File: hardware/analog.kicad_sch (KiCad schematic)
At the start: 13 parts

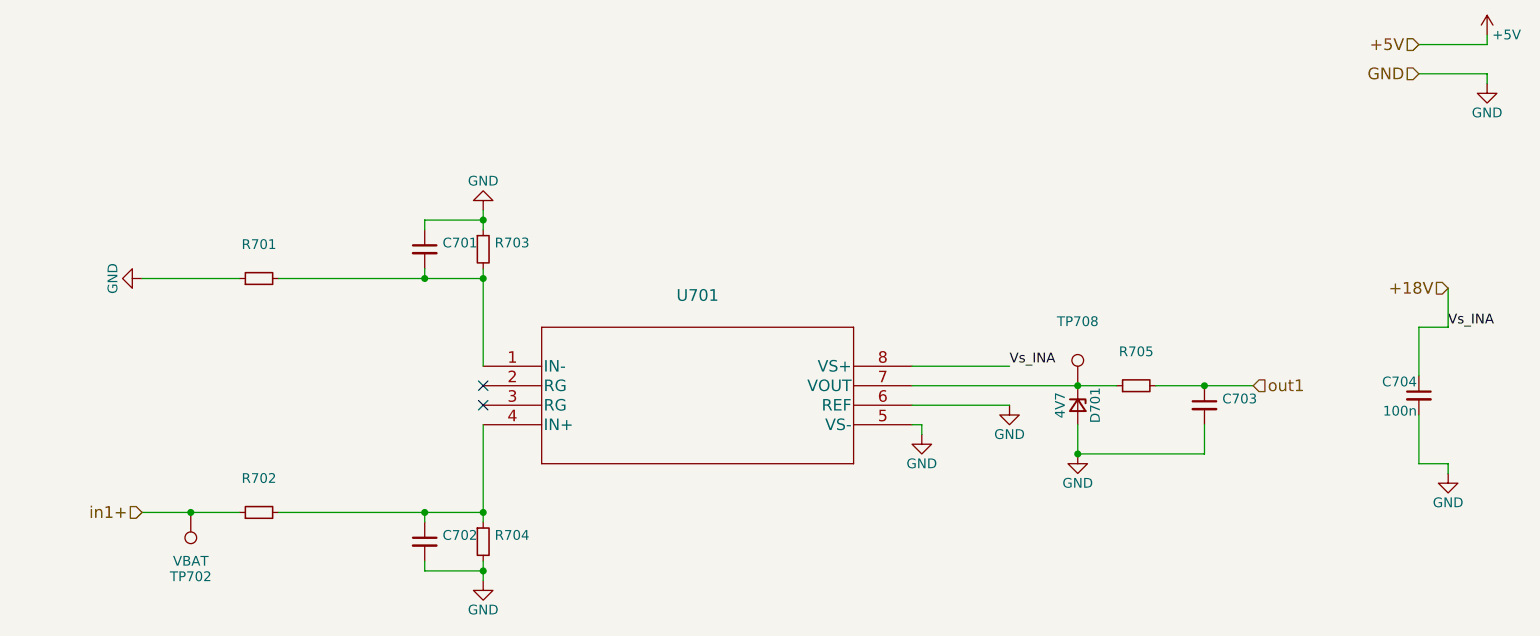
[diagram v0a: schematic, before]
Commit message: hardware: K78L15 to supply INA826 and other changes
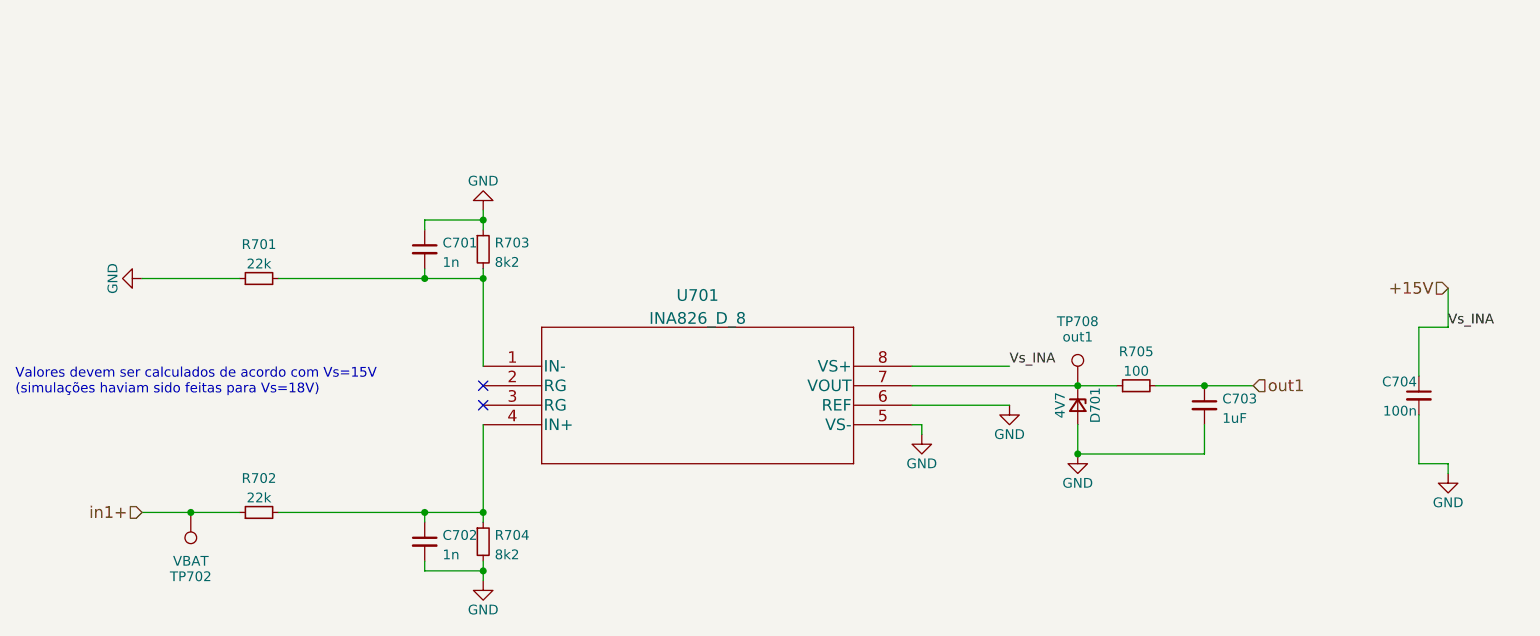
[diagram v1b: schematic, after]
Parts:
- C701, C702: value (none) -> 1n; footprint (none) -> Capacitor_SMD:C_0805_2012Metric_Pad1.18x1.45mm_HandSolder
- C703: value (none) -> 1uF; footprint (none) -> Capacitor_SMD:C_1206_3216Metric_Pad1.33x1.80mm_HandSolder
- R701, R702: value (none) -> 22k; footprint (none) -> Resistor_SMD:R_0805_2012Metric_Pad1.20x1.40mm_HandSolder
- R703, R704: value (none) -> 8k2; footprint (none) -> Resistor_SMD:R_0805_2012Metric_Pad1.20x1.40mm_HandSolder
- R705: value (none) -> 100; footprint (none) -> Resistor_SMD:R_0805_2012Metric_Pad1.20x1.40mm_HandSolder
- TP708: value (none) -> out1; footprint (none) -> TestPoint:TestPoint_Pad_2.0x2.0mm
- U701: value (none) -> INA826_D_8; footprint (none) -> Package_SO:SOIC-8_3.9x4.9mm_P1.27mm
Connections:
- net +18V renamed +15V
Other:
- note added: "Valores devem ser calculados de acordo com Vs=15V (simulações haviam sido feitas para Vs=18V)"
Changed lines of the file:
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@@
-    (stroke (width 0) (type default) (color 0 0 0 0))
-  )
-  (wire (pts (xy 251.46 57.15) (xy 242.57 57.15))
     (stroke (width 0) (type default) (color 0 0 0 0))
   )
@@
     (stroke (width 0) (type default) (color 0 0 0 0))
   )
-  (wire (pts (xy 251.46 55.88) (xy 251.46 57.15))
-    (stroke (width 0) (type default) (color 0 0 0 0))
-  )
   (wire (pts (xy 120.65 125.73) (xy 120.65 124.46))
     (stroke (width 0) (type default) (color 0 0 0 0))
@@
     (stroke (width 0) (type default) (color 0 0 0 0))
   )
-  (wire (pts (xy 251.46 60.96) (xy 251.46 62.23))
-    (stroke (width 0) (type default) (color 0 0 0 0))
-  )
   (wire (pts (xy 82.55 118.11) (xy 88.9 118.11))
     (stroke (width 0) (type default) (color 0 0 0 0))
   )
-  (wire (pts (xy 242.57 60.96) (xy 251.46 60.96))
-    (stroke (width 0) (type default) (color 0 0 0 0))
-  )
   (wire (pts (xy 113.03 125.73) (xy 120.65 125.73))
     (stroke (width 0) (type default) (color 0 0 0 0))
@@
   (wire (pts (xy 246.38 111.76) (xy 242.57 111.76))
     (stroke (width 0) (type default) (color 0 0 0 0))
+  )
+  (text "Valores devem ser calculados de acordo com Vs=15V\n(simulações haviam sido feitas para Vs=18V)"
+    (at 59.69 102.87 0)
+    (effects (font (size 1.27 1.27)) (justify left bottom))
   )
   (label "Vs_INA" (at 246.38 93.98 0)
@@
     (effects (font (size 1.524 1.524)) (justify right))
   )
-  (hierarchical_label "+5V" (shape input) (at 242.57 57.15 180)
-    (effects (font (size 1.524 1.524)) (justify right))
-  )
-  (hierarchical_label "+18V" (shape input) (at 246.38 88.9 180)
-    (effects (font (size 1.524 1.524)) (justify right))
-  )
-  (hierarchical_label "GND" (shape input) (at 242.57 60.96 180)
+  (hierarchical_label "+15V" (shape input) (at 246.38 88.9 180)
     (effects (font (size 1.524 1.524)) (justify right))
   )
@@
     (in_bom yes) (on_board yes) (fields_autoplaced)
     (property "Reference" "R702" (id 0) (at 91.44 113.6736 90))
-    (property "Value" "" (id 1) (at 91.44 116.2105 90))
-    (property "Footprint" "" (id 2) (at 91.44 118.11 0)
+    (property "Value" "22k" (id 1) (at 91.44 116.2105 90))
+    (property "Footprint" "Resistor_SMD:R_0805_2012Metric_Pad1.20x1.40mm_HandSolder" (id 2) (at 91.44 118.11 0)
       (effects (font (size 1.27 1.27)) hide)
     )
@@
       (effects (font (size 1.524 1.524)))
     )
-    (property "Value" "" (id 1) (at 148.59 92.8258 0)
+    (property "Value" "INA826_D_8" (id 1) (at 148.59 92.8258 0)
       (effects (font (size 1.524 1.524)))
     )
-    (property "Footprint" "" (id 2) (at 148.59 92.964 0)
+    (property "Footprint" "Package_SO:SOIC-8_3.9x4.9mm_P1.27mm" (id 2) (at 148.59 92.964 0)
       (effects (font (size 1.524 1.524)) hide)
     )
@@
       (effects (font (size 1.27 1.27)) (justify left))
     )
-    (property "Value" "" (id 1) (at 115.3541 123.6285 0)
-      (effects (font (size 1.27 1.27)) (justify left))
-    )
-    (property "Footprint" "" (id 2) (at 113.03 121.92 0)
+    (property "Value" "1n" (id 1) (at 115.3541 123.6285 0)
+      (effects (font (size 1.27 1.27)) (justify left))
+    )
+    (property "Footprint" "Capacitor_SMD:C_0805_2012Metric_Pad1.18x1.45mm_HandSolder" (id 2) (at 113.03 121.92 0)
       (effects (font (size 1.27 1.27)) hide)
     )
@@
       (effects (font (size 1.27 1.27)) (justify left))
     )
-    (property "Value" "" (id 1) (at 115.3541 85.5285 0)
-      (effects (font (size 1.27 1.27)) (justify left))
-    )
-    (property "Footprint" "" (id 2) (at 113.03 83.82 0)
+    (property "Value" "1n" (id 1) (at 115.3541 85.5285 0)
+      (effects (font (size 1.27 1.27)) (justify left))
+    )
+    (property "Footprint" "Capacitor_SMD:C_0805_2012Metric_Pad1.18x1.45mm_HandSolder" (id 2) (at 113.03 83.82 0)
       (effects (font (size 1.27 1.27)) hide)
     )
@@
       (effects (font (size 1.27 1.27)) (justify bottom))
     )
-    (property "Value" "" (id 1) (at 198.12 95.25 0))
-    (property "Footprint" "" (id 2) (at 198.12 101.6 0)
+    (property "Value" "out1" (id 1) (at 198.12 95.25 0))
+    (property "Footprint" "TestPoint:TestPoint_Pad_2.0x2.0mm" (id 2) (at 198.12 101.6 0)
       (effects (font (size 1.27 1.27)) hide)
     )
@@
     (in_bom yes) (on_board yes) (fields_autoplaced)
     (property "Reference" "R701" (id 0) (at 91.44 83.1936 90))
-    (property "Value" "" (id 1) (at 91.44 85.7305 90))
-    (property "Footprint" "" (id 2) (at 91.44 87.63 0)
+    (property "Value" "22k" (id 1) (at 91.44 85.7305 90))
+    (property "Footprint" "Resistor_SMD:R_0805_2012Metric_Pad1.20x1.40mm_HandSolder" (id 2) (at 91.44 87.63 0)
       (effects (font (size 1.27 1.27)) hide)
     )
@@
     (in_bom yes) (on_board yes) (fields_autoplaced)
     (property "Reference" "R705" (id 0) (at 205.74 97.1636 90))
-    (property "Value" "" (id 1) (at 205.74 99.7005 90))
-    (property "Footprint" "" (id 2) (at 205.74 101.6 0)
+    (property "Value" "100" (id 1) (at 205.74 99.7005 90))
+    (property "Footprint" "Resistor_SMD:R_0805_2012Metric_Pad1.20x1.40mm_HandSolder" (id 2) (at 205.74 101.6 0)
       (effects (font (size 1.27 1.27)) hide)
     )
@@
       (effects (font (size 1.27 1.27)) (justify left))
     )
-    (property "Value" "" (id 1) (at 216.9541 105.8485 0)
-      (effects (font (size 1.27 1.27)) (justify left))
-    )
-    (property "Footprint" "" (id 2) (at 214.63 104.14 0)
+    (property "Value" "1uF" (id 1) (at 216.9541 105.8485 0)
+      (effects (font (size 1.27 1.27)) (justify left))
+    )
+    (property "Footprint" "Capacitor_SMD:C_1206_3216Metric_Pad1.33x1.80mm_HandSolder" (id 2) (at 214.63 104.14 0)
       (effects (font (size 1.27 1.27)) hide)
     )
@@
       (effects (font (size 1.27 1.27)) (justify left))
     )
-    (property "Value" "" (id 1) (at 122.1486 123.6222 0)
-      (effects (font (size 1.27 1.27)) (justify left))
-    )
-    (property "Footprint" "" (id 2) (at 120.65 121.92 0)
+    (property "Value" "8k2" (id 1) (at 122.1486 123.6222 0)
+      (effects (font (size 1.27 1.27)) (justify left))
+    )
+    (property "Footprint" "Resistor_SMD:R_0805_2012Metric_Pad1.20x1.40mm_HandSolder" (id 2) (at 120.65 121.92 0)
       (effects (font (size 1.27 1.27)) hide)
     )
@@
       (effects (font (size 1.27 1.27)) (justify left))
     )
-    (property "Value" "" (id 1) (at 122.1486 85.5222 0)
-      (effects (font (size 1.27 1.27)) (justify left))
-    )
-    (property "Footprint" "" (id 2) (at 120.65 83.82 0)
+    (property "Value" "8k2" (id 1) (at 122.1486 85.5222 0)
+      (effects (font (size 1.27 1.27)) (justify left))
+    )
+    (property "Footprint" "Resistor_SMD:R_0805_2012Metric_Pad1.20x1.40mm_HandSolder" (id 2) (at 120.65 83.82 0)
       (effects (font (size 1.27 1.27)) hide)
     )
@@
     (pin "2")
   )
-  (symbol (lib_id "power:+5V") (at 251.46 55.88 0) (unit 1)
-    (in_bom yes) (on_board yes)
-    (property "Reference" "#PWR0707" (id 0) (at 251.46 59.69 0)
-      (effects (font (size 1.27 1.27)) hide)
-    )
-    (property "Value" "+5V" (id 1) (at 254 55.88 0))
-    (property "Footprint" "" (id 2) (at 251.46 55.88 0)
-      (effects (font (size 1.27 1.27)) hide)
-    )
-    (property "Datasheet" "" (id 3) (at 251.46 55.88 0)
-      (effects (font (size 1.27 1.27)) hide)
-    )
-    (pin "1")
-  )
-  (symbol (lib_id "power:GND") (at 251.46 62.23 0) (unit 1)
-    (in_bom yes) (on_board yes)
-    (property "Reference" "#PWR0708" (id 0) (at 251.46 68.58 0)
-      (effects (font (size 1.27 1.27)) hide)
-    )
-    (property "Value" "GND" (id 1) (at 251.46 66.04 0))
-    (property "Footprint" "" (id 2) (at 251.46 62.23 0)
-      (effects (font (size 1.27 1.27)) hide)
-    )
-    (property "Datasheet" "" (id 3) (at 251.46 62.23 0)
-      (effects (font (size 1.27 1.27)) hide)
-    )
-    (pin "1")
-  )
 )
